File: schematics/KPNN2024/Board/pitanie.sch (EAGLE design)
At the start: 31 parts

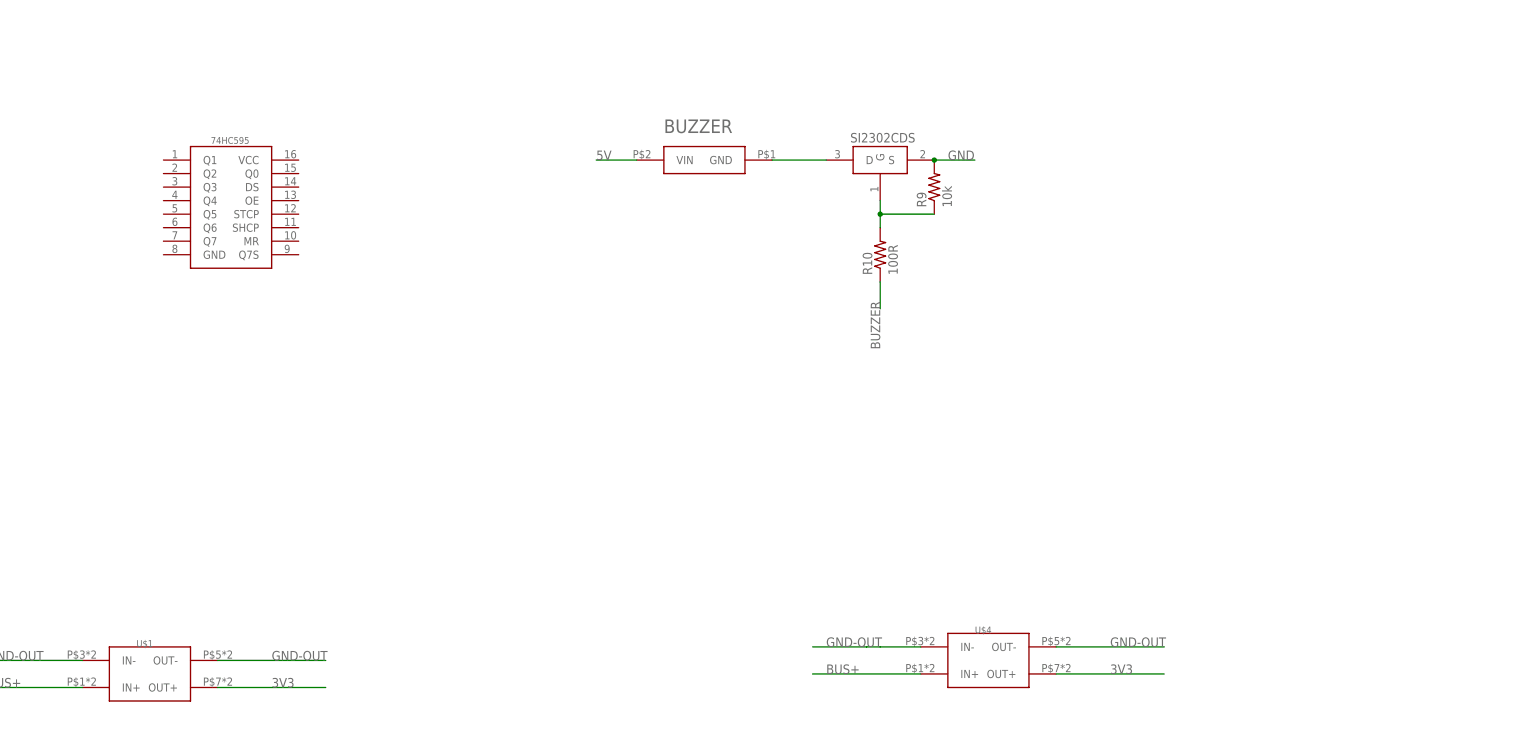
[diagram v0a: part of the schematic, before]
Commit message: Добавлена плата питания
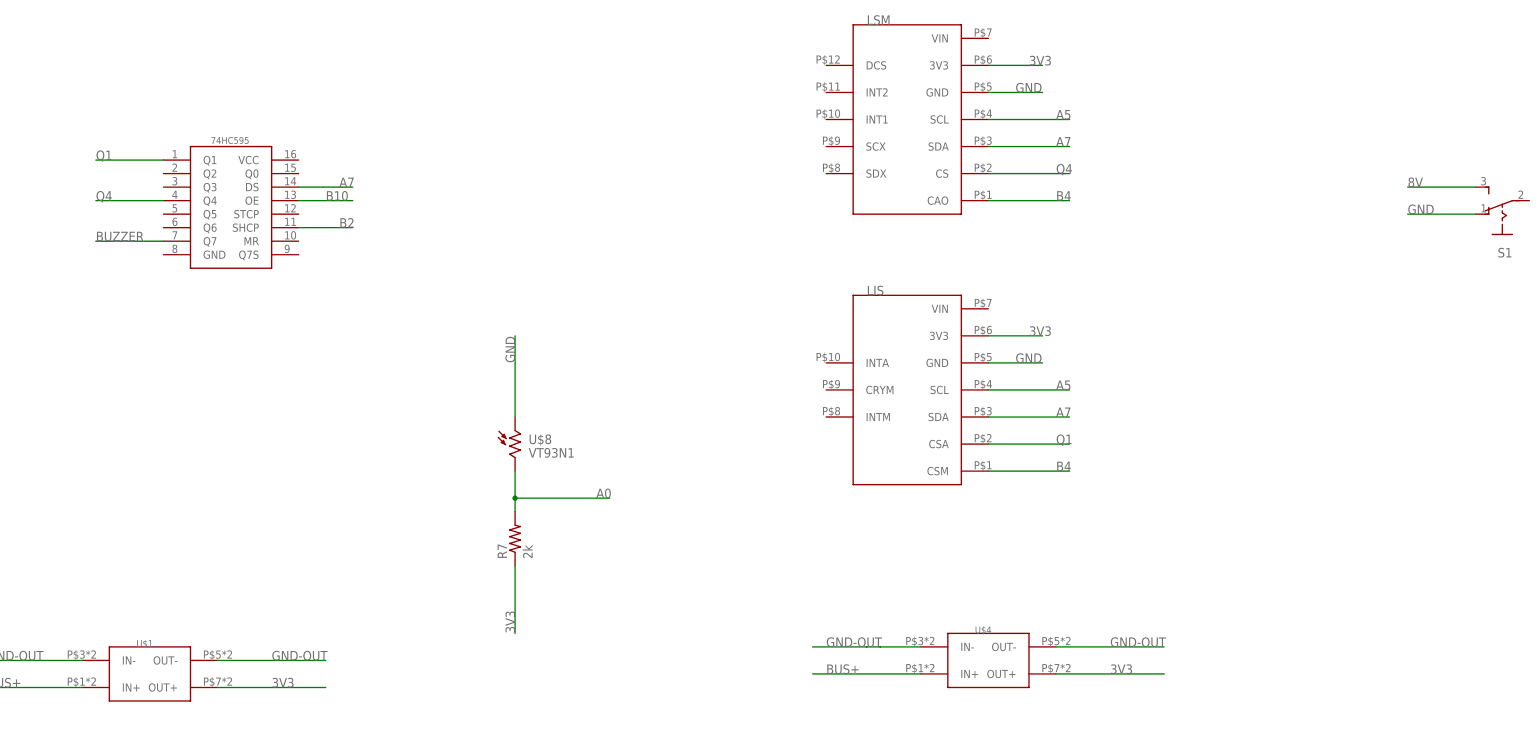
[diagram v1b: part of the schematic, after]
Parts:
- removed BUZZER: BUZZERS8R6, UNKNOWN-2024:BUZZERS8R6
- removed R10: 100R, rcl:R-US_R0603
- removed R9: 10k, rcl:R-US_R0603
- removed U$20: SI2302CDS, CanCubeSat:SI2302CDS
- added LIS: LIS3MDL-GY, CanCubeSat:LIS3MDL-GY
- added LSM: LSM6DS3-GY, UNKNOWN-2024:LSM6DS3-GY
- added R7: 2k, rcl:R-US_R0603
- added S1: (no value), UNKNOWN-2024:UNICS-SWITCHSS_12D11
- added U$8: VT93N1, KNPN-2023:VT93N1
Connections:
- removed net 5V: BUZZER.VIN
- removed net N$13: BUZZER.GND, U$20.D
- removed net N$14: R10.2, R9.1, U$20.G
- new net 8V: S1.S
- new net A0: R7.2, U$8.2
- new net A5: LIS.SCL, LSM.SCL
- new net A7: LIS.SDA, LSM.SDA, U$7.DS
- new net B10: U$7.OE
- new net B2: U$7.SHCP
- new net B4: LIS.CSM, LSM.CAO
- new net Q1: LIS.CSA, U$7.Q1
- new net Q4: LSM.CS, U$7.Q4
- net 3V3: now also LIS.3V3, LSM.3V3, R7.1
- net BUZZER: now also U$7.Q7; no longer R10.1
- net GND: now also LIS.GND, LSM.GND, S1.O, U$8.1; no longer R9.2, U$20.S

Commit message: я смотрел рика и морти вместо работать
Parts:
- added R8: 1k, rcl:R-US_R0603
- added TMC: DRIVER_TMC2209, UNKNOWN-2024:DRIVER_TMC2209
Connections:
- new net 5V: TMC.P$16
- new net A2: R8.2
- new net A3: R8.1, TMC.P$4
- net GND: now also TMC.P$15, TMC.P$9
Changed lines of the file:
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@@
 <setting verticaltext="up"/>
 </settings>
-<grid distance="0.1" unitdist="inch" unit="inch" style="lines" multiple="1" display="no" altdistance="0.01" altunitdist="inch" altunit="inch"/>
+<grid distance="1" unitdist="mm" unit="mm" style="lines" multiple="1" display="no" altdistance="0.05" altunitdist="mm" altunit="mm"/>
 <layers>
 <layer number="1" name="Top" color="4" fill="1" visible="no" active="no"/>
@@
 <part name="LIS" library="CanCubeSat" deviceset="LIS3MDL-GY" device=""/>
 <part name="R7" library="rcl" library_urn="urn:adsk.eagle:library:334" deviceset="R-US_" device="R0603" package3d_urn="urn:adsk.eagle:package:23555/3" value="2k"/>
+<part name="TMC" library="UNKNOWN-2024" deviceset="DRIVER_TMC2209" device=""/>
+<part name="R8" library="rcl" library_urn="urn:adsk.eagle:library:334" deviceset="R-US_" device="R0603" package3d_urn="urn:adsk.eagle:package:23555/3" value="1k"/>
 </parts>
 <sheets>
@@
 <attribute name="NAME" x="117.8814" y="85.09" size="1.778" layer="95" rot="R90"/>
 <attribute name="VALUE" x="122.682" y="85.09" size="1.778" layer="96" rot="R90"/>
+</instance>
+<instance part="TMC" gate="G$1" x="362" y="78" smashed="yes"/>
+<instance part="R8" gate="G$1" x="345.22" y="94.94" smashed="yes" rot="R90">
+<attribute name="NAME" x="343.7214" y="91.13" size="1.778" layer="95" rot="R90"/>
+<attribute name="VALUE" x="348.522" y="91.13" size="1.778" layer="96" rot="R90"/>
 </instance>
 </instances>
@@
 <label x="213.36" y="121.92" size="1.778" layer="95"/>
 </segment>
+<segment>
+<pinref part="TMC" gate="G$1" pin="P$9"/>
+<wire x1="382.4" y1="79.4" x2="398.244984375" y2="79.4" width="0.1524" layer="91"/>
+<wire x1="398.244984375" y1="79.4" x2="398.244984375" y2="79.3966125" width="0.1524" layer="91"/>
+<label x="393.112159375" y="79.48539375" size="1.778" layer="95"/>
+</segment>
+<segment>
+<pinref part="TMC" gate="G$1" pin="P$15"/>
+<wire x1="382.4" y1="94.1" x2="398" y2="94.1" width="0.1524" layer="91"/>
+<wire x1="398" y1="94.1" x2="398" y2="94" width="0.1524" layer="91"/>
+<label x="393" y="94" size="1.778" layer="95"/>
+</segment>
 </net>
 <net name="8V" class="0">
@@
 </segment>
 </net>
+<net name="A3" class="0">
+<segment>
+<pinref part="TMC" gate="G$1" pin="P$4"/>
+<wire x1="357" y1="89.25" x2="345" y2="89.25" width="0.1524" layer="91"/>
+<wire x1="345" y1="89.25" x2="345" y2="89" width="0.1524" layer="91"/>
+<wire x1="345" y1="89" x2="333" y2="89" width="0.1524" layer="91"/>
+<pinref part="R8" gate="G$1" pin="1"/>
+<wire x1="345" y1="89.25" x2="345" y2="89.86" width="0.1524" layer="91"/>
+<wire x1="345" y1="89.86" x2="345.22" y2="89.86" width="0.1524" layer="91"/>
+<label x="333" y="89" size="1.778" layer="95"/>
+</segment>
+</net>
+<net name="A2" class="0">
+<segment>
+<pinref part="R8" gate="G$1" pin="2"/>
+<wire x1="345.22" y1="100.02" x2="334" y2="100.02" width="0.1524" layer="91"/>
+<wire x1="334" y1="100.02" x2="334" y2="100" width="0.1524" layer="91"/>
+<label x="334" y="100" size="1.778" layer="95"/>
+</segment>
+</net>
+<net name="5V" class="0">
+<segment>
+<pinref part="TMC" gate="G$1" pin="P$16"/>
+<wire x1="382.4" y1="96.55" x2="397.958121875" y2="96.55" width="0.1524" layer="91"/>
+<wire x1="397.958121875" y1="96.55" x2="397.958121875" y2="96.542290625" width="0.1524" layer="91"/>
+<label x="395.55" y="96.6" size="1.778" layer="95"/>
+</segment>
+</net>

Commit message: ааа платы платы полигоны разводка платы ааааа
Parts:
- C2, C6, C7: device rcl:C-USC0603 -> rcl:C-USC1206
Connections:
- removed net N$6: C5.1, C6.2, C7.2, R3.2, U$3.1
- net 3V3: now also C5.1, C6.2, C7.2, R3.2, U$3.1
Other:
- moved on the sheet: R4

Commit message: авыпльдыф
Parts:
- C13, C14, C9: device rcl:C-USC0603 -> rcl:C-USC1206
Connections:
- removed net N$12: C12.1, C13.2, C14.2, R6.2, U$6.1
- net 3V3: now also C12.1, C13.2, C14.2, R6.2, U$6.1

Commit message: amogus
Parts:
- removed R8: 1k, rcl:R-US_R0603
- added U$10: PBS_SMD_X13, UNKNOWN-2024:PBS_SMD_X13
- added U$11: LIS3MDL, UNKNOWN-2024:LIS3MDL
- added U$9: PBS_SMD_X9, UNKNOWN-2024:PBS_SMD_X9
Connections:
- net A0 renamed FOTO
- net B10 renamed OE_SR
- removed net A2: R8.2
- removed net A3: R8.1, TMC.P$4
- removed net A5: LIS.SCL, LSM.SCL
- removed net A7: LIS.SDA, LSM.SDA, U$7.DS
- removed net B2: U$7.SHCP
- removed net B4: LIS.CSM, LSM.CAO
- new net DIR_DRIVER: TMC.P$8
- new net LATCH_SR: U$7.STCP
- new net MISO_SR: LSM.CAO, U$11.SDO
- new net MOSI_SR: LSM.SDA, U$11.SDA, U$7.DS
- new net SCK_SR: LSM.SCL, U$11.SCL, U$7.SHCP
- new net STEP_DRIVER: TMC.P$7
- net 3V3: now also U$11.UCC, U$7.VCC; no longer LIS.3V3
- net GND: now also U$11.GND, U$7.GND; no longer LIS.GND
- net Q1: now also U$11.CS; no longer LIS.CSA
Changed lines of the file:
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@@
 <part name="R7" library="rcl" library_urn="urn:adsk.eagle:library:334" deviceset="R-US_" device="R0603" package3d_urn="urn:adsk.eagle:package:23555/3" value="2k"/>
 <part name="TMC" library="UNKNOWN-2024" deviceset="DRIVER_TMC2209" device=""/>
-<part name="R8" library="rcl" library_urn="urn:adsk.eagle:library:334" deviceset="R-US_" device="R0603" package3d_urn="urn:adsk.eagle:package:23555/3" value="1k"/>
+<part name="U$9" library="UNKNOWN-2024" deviceset="PBS_SMD_X9" device=""/>
+<part name="U$10" library="UNKNOWN-2024" deviceset="PBS_SMD_X13" device=""/>
+<part name="U$11" library="UNKNOWN-2024" deviceset="LIS3MDL" device=""/>
 </parts>
 <sheets>
@@
 </instance>
 <instance part="TMC" gate="G$1" x="362" y="78" smashed="yes"/>
-<instance part="R8" gate="G$1" x="345.22" y="94.94" smashed="yes" rot="R90">
-<attribute name="NAME" x="343.7214" y="91.13" size="1.778" layer="95" rot="R90"/>
-<attribute name="VALUE" x="348.522" y="91.13" size="1.778" layer="96" rot="R90"/>
+<instance part="U$9" gate="G$1" x="340.36" y="27.94" smashed="yes">
+<attribute name="NAME" x="334.01" y="41.275" size="1.778" layer="95"/>
+<attribute name="VALUE" x="334.01" y="12.7" size="1.778" layer="96"/>
+</instance>
+<instance part="U$10" gate="G$1" x="391.16" y="22.86" smashed="yes">
+<attribute name="NAME" x="384.81" y="41.275" size="1.778" layer="95"/>
+<attribute name="VALUE" x="384.81" y="2.54" size="1.778" layer="96"/>
+</instance>
+<instance part="U$11" gate="G$1" x="256.54" y="111.76" smashed="yes">
+<attribute name="NAME" x="246.38" y="132.08" size="1.27" layer="95"/>
+<attribute name="VALUE" x="246.38" y="83.82" size="1.27" layer="96"/>
 </instance>
 </instances>
@@
 </segment>
 <segment>
-<pinref part="LIS" gate="G$1" pin="3V3"/>
-<wire x1="208.28" y1="127" x2="218.44" y2="127" width="0.1524" layer="91"/>
-<label x="215.9" y="127" size="1.778" layer="95"/>
+<pinref part="U$11" gate="G$1" pin="UCC"/>
+<wire x1="241.3" y1="127" x2="233.68" y2="127" width="0.1524" layer="91"/>
+<label x="233.68" y="127" size="1.778" layer="95"/>
 </segment>
 <segment>
@@
 <label x="198.12" y="33.02" size="1.778" layer="95"/>
 </segment>
+<segment>
+<pinref part="U$7" gate="G$1" pin="VCC"/>
+<wire x1="78.74" y1="160.02" x2="88.9" y2="160.02" width="0.1524" layer="91"/>
+<label x="83.82" y="160.02" size="1.778" layer="95"/>
+</segment>
 </net>
 <net name="BUS+" class="0">
@@
 </segment>
 <segment>
-<pinref part="LIS" gate="G$1" pin="GND"/>
-<wire x1="208.28" y1="121.92" x2="218.44" y2="121.92" width="0.1524" layer="91"/>
-<label x="213.36" y="121.92" size="1.778" layer="95"/>
+<label x="233.68" y="121.92" size="1.778" layer="95"/>
+<pinref part="U$11" gate="G$1" pin="GND"/>
+<wire x1="241.3" y1="121.92" x2="233.68" y2="121.92" width="0.1524" layer="91"/>
 </segment>
 <segment>
@@
 <label x="393" y="94" size="1.778" layer="95"/>
 </segment>
+<segment>
+<pinref part="U$7" gate="G$1" pin="GND"/>
+<wire x1="53.34" y1="142.24" x2="40.64" y2="142.24" width="0.1524" layer="91"/>
+<label x="40.64" y="142.24" size="1.778" layer="95"/>
+</segment>
 </net>
 <net name="8V" class="0">
@@
 </segment>
 </net>
-<net name="A0" class="0">
+<net name="FOTO" class="0">
 <segment>
 <pinref part="U$8" gate="G$1" pin="2"/>
@@
 </segment>
 </net>
-<net name="A7" class="0">
-<segment>
-<pinref part="LIS" gate="G$1" pin="SDA"/>
-<wire x1="208.28" y1="111.76" x2="223.52" y2="111.76" width="0.1524" layer="91"/>
-<label x="220.98" y="111.76" size="1.778" layer="95"/>
-</segment>
-<segment>
-<pinref part="U$7" gate="G$1" pin="DS"/>
-<wire x1="78.74" y1="154.94" x2="88.9" y2="154.94" width="0.1524" layer="91"/>
-<label x="86.36" y="154.94" size="1.778" layer="95"/>
-</segment>
-<segment>
-<pinref part="LSM" gate="G$1" pin="SDA"/>
-<wire x1="208.28" y1="162.56" x2="223.52" y2="162.56" width="0.1524" layer="91"/>
-<label x="220.98" y="162.56" size="1.778" layer="95"/>
-</segment>
-</net>
-<net name="A5" class="0">
-<segment>
-<pinref part="LIS" gate="G$1" pin="SCL"/>
-<wire x1="208.28" y1="116.84" x2="223.52" y2="116.84" width="0.1524" layer="91"/>
-<label x="220.98" y="116.84" size="1.778" layer="95"/>
-</segment>
-<segment>
-<pinref part="LSM" gate="G$1" pin="SCL"/>
-<wire x1="208.28" y1="167.64" x2="223.52" y2="167.64" width="0.1524" layer="91"/>
-<label x="220.98" y="167.64" size="1.778" layer="95"/>
-</segment>
-</net>
-<net name="B10" class="0">
+<net name="OE_SR" class="0">
 <segment>
 <pinref part="U$7" gate="G$1" pin="OE"/>
@@
 </segment>
 </net>
-<net name="B2" class="0">
-<segment>
-<pinref part="U$7" gate="G$1" pin="SHCP"/>
-<wire x1="78.74" y1="147.32" x2="88.9" y2="147.32" width="0.1524" layer="91"/>
-<label x="86.36" y="147.32" size="1.778" layer="95"/>
-</segment>
-</net>
 <net name="Q1" class="0">
 <segment>
@@
 </segment>
 <segment>
-<pinref part="LIS" gate="G$1" pin="CSA"/>
-<wire x1="208.28" y1="106.68" x2="223.52" y2="106.68" width="0.1524" layer="91"/>
-<label x="220.98" y="106.68" size="1.778" layer="95"/>
+<label x="233.68" y="101.6" size="1.778" layer="95"/>
+<pinref part="U$11" gate="G$1" pin="CS"/>
+<wire x1="241.3" y1="101.6" x2="233.68" y2="101.6" width="0.1524" layer="91"/>
 </segment>
 </net>
@@
 </segment>
 </net>
-<net name="B4" class="0">
-<segment>
-<pinref part="LIS" gate="G$1" pin="CSM"/>
-<wire x1="208.28" y1="101.6" x2="223.52" y2="101.6" width="0.1524" layer="91"/>
-<label x="220.98" y="101.6" size="1.778" layer="95"/>
-</segment>
-<segment>
-<pinref part="LSM" gate="G$1" pin="CAO"/>
-<wire x1="208.28" y1="152.4" x2="223.52" y2="152.4" width="0.1524" layer="91"/>
-<label x="220.98" y="152.4" size="1.778" layer="95"/>
-</segment>
-</net>
 <net name="BUZZER" class="0">
 <segment>
@@
 <wire x1="53.34" y1="144.78" x2="40.64" y2="144.78" width="0.1524" layer="91"/>
 <label x="40.64" y="144.78" size="1.778" layer="95"/>
-</segment>
-</net>
-<net name="A3" class="0">
-<segment>
-<pinref part="TMC" gate="G$1" pin="P$4"/>
-<wire x1="357" y1="89.25" x2="345" y2="89.25" width="0.1524" layer="91"/>
-<wire x1="345" y1="89.25" x2="345" y2="89" width="0.1524" layer="91"/>
-<wire x1="345" y1="89" x2="333" y2="89" width="0.1524" layer="91"/>
-<pinref part="R8" gate="G$1" pin="1"/>
-<wire x1="345" y1="89.25" x2="345" y2="89.86" width="0.1524" layer="91"/>
-<wire x1="345" y1="89.86" x2="345.22" y2="89.86" width="0.1524" layer="91"/>
-<label x="333" y="89" size="1.778" layer="95"/>
-</segment>
-</net>
-<net name="A2" class="0">
-<segment>
-<pinref part="R8" gate="G$1" pin="2"/>
-<wire x1="345.22" y1="100.02" x2="334" y2="100.02" width="0.1524" layer="91"/>
-<wire x1="334" y1="100.02" x2="334" y2="100" width="0.1524" layer="91"/>
-<label x="334" y="100" size="1.778" layer="95"/>
 </segment>
 </net>
@@
 </segment>
 </net>
+<net name="LATCH_SR" class="0">
+<segment>
+<pinref part="U$7" gate="G$1" pin="STCP"/>
+<wire x1="78.74" y1="149.86" x2="88.9" y2="149.86" width="0.1524" layer="91"/>
+<label x="78.74" y="149.86" size="1.778" layer="95"/>
+</segment>
+</net>
+<net name="SCK_SR" class="0">
+<segment>
+<label x="228.6" y="116.84" size="1.778" layer="95"/>
+<pinref part="U$11" gate="G$1" pin="SCL"/>
+<wire x1="241.3" y1="116.84" x2="228.6" y2="116.84" width="0.1524" layer="91"/>
+</segment>
+<segment>
+<pinref part="LSM" gate="G$1" pin="SCL"/>
+<wire x1="208.28" y1="167.64" x2="223.52" y2="167.64" width="0.1524" layer="91"/>
+<label x="220.98" y="167.64" size="1.778" layer="95"/>
+</segment>
+<segment>
+<pinref part="U$7" gate="G$1" pin="SHCP"/>
+<wire x1="78.74" y1="147.32" x2="88.9" y2="147.32" width="0.1524" layer="91"/>
+<label x="86.36" y="147.32" size="1.778" layer="95"/>
+</segment>
+</net>
+<net name="MOSI_SR" class="0">
+<segment>
+<label x="228.6" y="111.76" size="1.778" layer="95"/>
+<pinref part="U$11" gate="G$1" pin="SDA"/>
+<wire x1="241.3" y1="111.76" x2="228.6" y2="111.76" width="0.1524" layer="91"/>
+</segment>
+<segment>
+<pinref part="LSM" gate="G$1" pin="SDA"/>
+<wire x1="208.28" y1="162.56" x2="223.52" y2="162.56" width="0.1524" layer="91"/>
+<label x="220.98" y="162.56" size="1.778" layer="95"/>
+</segment>
+<segment>
+<pinref part="U$7" gate="G$1" pin="DS"/>
+<wire x1="78.74" y1="154.94" x2="88.9" y2="154.94" width="0.1524" layer="91"/>
+<label x="86.36" y="154.94" size="1.778" layer="95"/>
+</segment>
+</net>
+<net name="STEP_DRIVER" class="0">
+<segment>
+<pinref part="TMC" gate="G$1" pin="P$7"/>
+<wire x1="357" y1="81.9" x2="343.916" y2="81.9" width="0.1524" layer="91"/>
+<wire x1="343.916" y1="81.9" x2="343.916" y2="82.296" width="0.1524" layer="91"/>
+<label x="336.296" y="82.55" size="1.778" layer="95"/>
+</segment>
+</net>
+<net name="DIR_DRIVER" class="0">
+<segment>
+<pinref part="TMC" gate="G$1" pin="P$8"/>
+<wire x1="357" y1="79.45" x2="343.916" y2="79.45" width="0.1524" layer="91"/>
+<wire x1="343.916" y1="79.45" x2="343.916" y2="79.756" width="0.1524" layer="91"/>
+<label x="336.55" y="79.756" size="1.778" layer="95"/>
+</segment>
+</net>
+<net name="MISO_SR" class="0">
+<segment>
+<label x="228.6" y="106.68" size="1.778" layer="95"/>
+<pinref part="U$11" gate="G$1" pin="SDO"/>
+<wire x1="241.3" y1="106.68" x2="233.68" y2="106.68" width="0.1524" layer="91"/>
+</segment>
+<segment>
+<pinref part="LSM" gate="G$1" pin="CAO"/>
+<wire x1="208.28" y1="152.4" x2="223.52" y2="152.4" width="0.1524" layer="91"/>
+<label x="220.98" y="152.4" size="1.778" layer="95"/>
+</segment>
+</net>
